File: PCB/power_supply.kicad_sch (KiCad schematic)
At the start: 25 parts, among them J1 Barrel_Jack_Switch, Q401 PMOS, U204 NCP431, U3 LDK320, U302 LMR54410DBVR, U402 TLV3542

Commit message: footprints
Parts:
- removed U402: TLV3542, w-ic:SOIC-8, symbol w-analog-ic:TLV3542
- added U403: TLV3542, w-ic:SOIC-8, symbol w-analog-ic:TLV3542
- C401: renamed from C1; footprint (none) -> Capacitor_SMD:C_0603_1608Metric
- C402: renamed from C3; footprint (none) -> Capacitor_THT:C_Radial_D6.3mm_H11.0mm_P2.50mm
- C403: renamed from C2; footprint (none) -> Capacitor_SMD:C_0603_1608Metric
- C404: renamed from C5; footprint (none) -> Capacitor_SMD:C_0603_1608Metric
- C405: renamed from C4; footprint (none) -> Capacitor_THT:C_Radial_D6.3mm_H11.0mm_P2.50mm
- C409: renamed from C6; footprint (none) -> Capacitor_SMD:C_0603_1608Metric
- C411: renamed from C7; footprint (none) -> Capacitor_SMD:C_0603_1608Metric
- C412: renamed from C8; footprint (none) -> Capacitor_SMD:C_0603_1608Metric
- D401: footprint (none) -> LED_SMD:LED_0603_1608Metric
- FB401: renamed from FB1; value FerriteBead -> 470R@100MHz; footprint (none) -> Inductor_SMD:L_0603_1608Metric; Store (none) -> https://cz.mouser.com/ProductDetail/TAIYO-YUDEN/FBMH1608HM4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
- J401: renamed from J1; footprint (none) -> w-connector:Barrel jack 6,4mm; Store (none) -> https://cz.mouser.com/ProductDetail/Adam-Tech/ADC-002-1?qs=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
- Q401: value PMOS -> DMP3125L; footprint (none) -> w-transistor:SOT23-3; Store (none) -> https://cz.mouser.com/ProductDetail/Diodes-Incorporated/DMP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
- R401, R404: footprint (none) -> Resistor_SMD:R_0603_1608Metric
- renumbered C303 to C406, C304 to C407, C308 to C408, C310 to C410, L301 to L401, U3 to U401, U302 to U402, U204 to U404
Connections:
- net +12V: now also R401.1; no longer R401.2
- net +5VA: now also U403.8 (V+)
- net GND: now also Q401.1 (G), U403.4 (V-); no longer Q401.2 (G)
- net GNDA: now also U403.1, U403.2 (-)
- net at D401.2 (A): now also R401.2; no longer R401.1
- net at R404.2, U404.1 (K), U404.2 (REF): now also U403.3 (+)
- net at J401.1: now also Q401.2 (D); no longer Q401.1 (D)
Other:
- moved on the sheet: C407, C410, Q401, R401, R402, R403

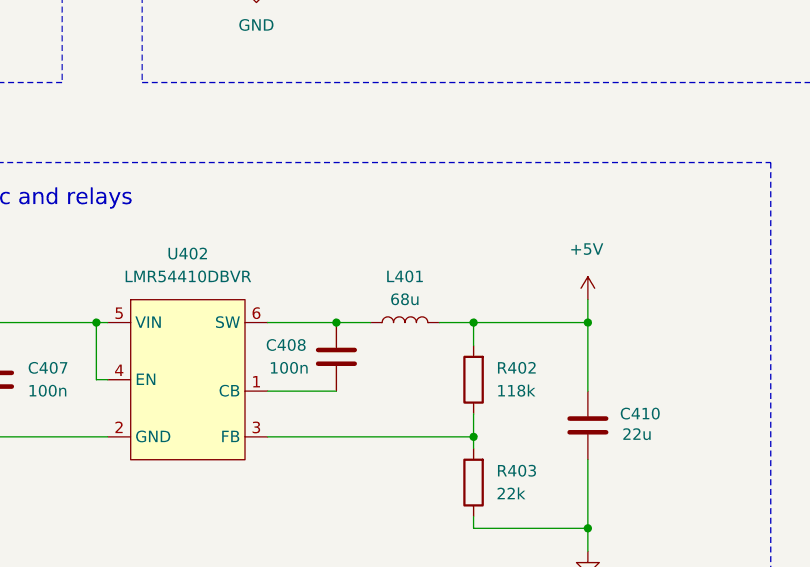
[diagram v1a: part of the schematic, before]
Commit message: footprints and overrange detector timing
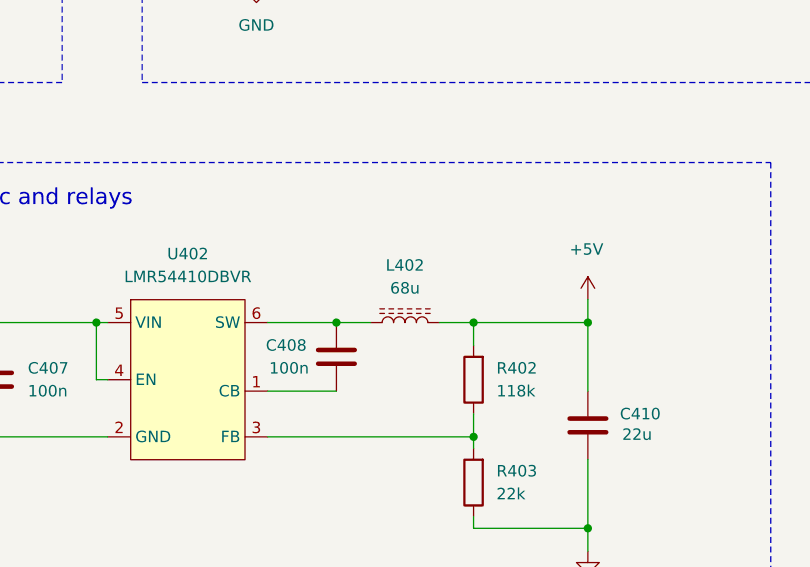
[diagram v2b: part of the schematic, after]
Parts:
- removed L401: 68u, symbol Device:L
- added L402: 68u, w-magnetics:Shielded L 6x6x4.2mm, symbol Device:L_Ferrite
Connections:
- net +5V: now also L402.2
- net at C408.2, U402.6 (SW): now also L402.1
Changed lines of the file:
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@@
-	)
-	(symbol
-		(lib_id "Device:L")
-		(at 201.93 114.3 90)
-		(unit 1)
-		(exclude_from_sim no)
-		(in_bom yes)
-		(on_board yes)
-		(dnp no)
-		(fields_autoplaced yes)
-		(property "Reference" "L401"
-			(at 201.93 109.22 90)
-			(effects
-				(font
-					(size 1.27 1.27)
-				)
-			)
-		)
-		(property "Value" "68u"
-			(at 201.93 111.76 90)
-			(effects
-				(font
-					(size 1.27 1.27)
-				)
-			)
-		)
-		(property "Footprint" ""
-			(at 201.93 114.3 0)
-			(effects
-				(font
-					(size 1.27 1.27)
-				)
-				(hide yes)
-			)
-		)
-		(property "Datasheet" "https://cz.mouser.com/datasheet/3/40/1/srn6045ta.pdf"
-			(at 201.93 114.3 0)
-			(effects
-				(font
-					(size 1.27 1.27)
-				)
-				(hide yes)
-			)
-		)
-		(property "Description" ""
-			(at 201.93 114.3 0)
-			(effects
-				(font
-					(size 1.27 1.27)
-				)
-				(hide yes)
-			)
-		)
-		(property "Store" "https://cz.mouser.com/ProductDetail/Bourns/SRN6045TA-680M?qs=Vt59ZOdFuWZwwb5da9XlfA%3D%3D"
-			(at 201.93 114.3 90)
-			(effects
-				(font
-					(size 1.27 1.27)
-				)
-				(hide yes)
-			)
-		)
-		(pin "1"
-		)
-		(pin "2"
-		)
-		(instances
-			(project "PCB"
-				(path "/8a6cedb2-c3ba-4f13-be40-fdd77ffb4e16/a8173f43-9291-44ee-92e5-00a0bb4b8099"
-					(reference "L401")
-					(unit 1)
-				)
-			)
-		)
 	)
 	(symbol
@@
 					(unit 1)
 				)
+			)
+		)
+	)
+	(symbol
+		(lib_id "Device:L_Ferrite")
+		(at 201.93 114.3 90)
+		(unit 1)
+		(exclude_from_sim no)
+		(in_bom yes)
+		(on_board yes)
+		(dnp no)
+		(fields_autoplaced yes)
+		(property "Reference" "L402"
+			(at 201.93 107.95 90)
+			(effects
+				(font
+					(size 1.27 1.27)
+				)
+			)
+		)
+		(property "Value" "68u"
+			(at 201.93 110.49 90)
+			(effects
+				(font
+					(size 1.27 1.27)
+				)
+			)
+		)
+		(property "Footprint" "w-magnetics:Shielded L 6x6x4.2mm"
+			(at 201.93 114.3 0)
+			(effects
+				(font
+					(size 1.27 1.27)
+				)
+				(hide yes)
+			)
+		)
+		(property "Datasheet" "https://cz.mouser.com/datasheet/3/40/1/srn6045ta.pdf"
+			(at 201.93 114.3 0)
+			(effects
+				(font
+					(size 1.27 1.27)
+				)
+				(hide yes)
+			)
+		)
+		(property "Description" "Inductor with ferrite core"
+			(at 201.93 114.3 0)
+			(effects
+				(font
+					(size 1.27 1.27)
+				)
+				(hide yes)
+			)
+		)
+		(property "Store" "https://cz.mouser.com/ProductDetail/Bourns/SRN6045TA-680M?qs=Vt59ZOdFuWZwwb5da9XlfA%3D%3D"
+			(at 201.93 114.3 90)
+			(effects
+				(font
+					(size 1.27 1.27)
+				)
+				(hide yes)
+			)
+		)
+		(pin "2"
+		)
+		(pin "1"
+		)
+		(instances
+			(project ""
+				(path "/8a6cedb2-c3ba-4f13-be40-fdd77ffb4e16/a8173f43-9291-44ee-92e5-00a0bb4b8099"
+					(reference "L402")
+					(unit 1)
+				)

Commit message: changes
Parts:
- removed U403: TLV3542, w-ic:SOIC-8, symbol w-analog-ic:TLV3542
- added U404: TLV9361xDBV, w-ic:SOT-23-5L, symbol Amplifier_Operational:TLV9301xDBV
- C411, C412: value 1u -> 100n
- renumbered C409 to C408, C408 to C409, L402 to L401, R404 to R402, R402 to R403, R403 to R404, U404 to U403
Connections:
- net GND2 is gone; now on net GND: C406.2, C407.2, C410.1, R404.1, U402.2 (GND)
- net +5VA: now also U404.5 (V+)
- net GND: now also C401.2, C403.2, U401.2 (GND), U404.2 (V-)
- net GNDA: now also U404.1, U404.3 (+)
- net at R402.2, U403.1 (K), U403.2 (REF): now also U404.4 (-)
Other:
- moved on the sheet: C408, C411, C412, R402, U403

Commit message: start of layout
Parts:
- removed U403: NCP431, w-ic:SOT-23, symbol Reference_Voltage:TL431DBZ
- added R405: 100k, Resistor_SMD:R_0603_1608Metric, symbol Device:R
- C410: footprint Capacitor_SMD:C_0603_1608Metric -> Capacitor_SMD:C_0805_2012Metric
- D401: footprint LED_SMD:LED_0603_1608Metric -> LED_THT:LED_D3.0mm_Clear
- R401: value 1k -> 4k7
- R402: value 4k7 -> 100k
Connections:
- net GND: now also R405.2
- net at R402.2, U404.4 (-): now also R405.1
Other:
- moved on the sheet: R402
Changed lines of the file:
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@@
 	)
 	(junction
-		(at 209.55 58.42)
+		(at 156.21 127)
 		(diameter 0)
 		(color 0 0 0 0)
 	)
 	(junction
-		(at 156.21 127)
+		(at 210.82 74.93)
 		(diameter 0)
 		(color 0 0 0 0)
@@
 	)
 	(junction
-		(at 115.57 46.99)
+		(at 210.82 58.42)
 		(diameter 0)
 		(color 0 0 0 0)
 	)
 	(junction
-		(at 86.36 46.99)
+		(at 115.57 46.99)
 		(diameter 0)
 		(color 0 0 0 0)
 	)
 	(junction
-		(at 209.55 74.93)
+		(at 86.36 46.99)
 		(diameter 0)
 		(color 0 0 0 0)
@@
 	)
 	(junction
-		(at 209.55 40.64)
-		(diameter 0)
-		(color 0 0 0 0)
-	)
-	(junction
 		(at 227.33 74.93)
 		(diameter 0)
@@
 	)
 	(junction
+		(at 210.82 40.64)
+		(diameter 0)
+		(color 0 0 0 0)
+	)
+	(junction
 		(at 209.55 114.3)
 		(diameter 0)
@@
 	(wire
 		(pts
-			(xy 209.55 40.64) (xy 227.33 40.64)
-		)
-		(stroke
-			(width 0)
-			(type default)
-		)
-	)
-	(wire
-		(pts
 			(xy 44.45 52.07) (xy 49.53 52.07)
 		)
@@
 	(wire
 		(pts
-			(xy 203.2 58.42) (xy 209.55 58.42)
-		)
-		(stroke
-			(width 0)
-			(type default)
-		)
-	)
-	(wire
-		(pts
-			(xy 203.2 64.77) (xy 203.2 58.42)
-		)
-		(stroke
-			(width 0)
-			(type default)
-		)
-	)
-	(wire
-		(pts
 			(xy 86.36 46.99) (xy 97.79 46.99)
 		)
@@
 	(wire
 		(pts
-			(xy 207.01 64.77) (xy 203.2 64.77)
-		)
-		(stroke
-			(width 0)
-			(type default)
-		)
-	)
-	(wire
-		(pts
 			(xy 237.49 55.88) (xy 246.38 55.88)
 		)
@@
 	(wire
 		(pts
-			(xy 209.55 40.64) (xy 209.55 46.99)
+			(xy 210.82 40.64) (xy 210.82 45.72)
 		)
 		(stroke
@@
 	(wire
 		(pts
-			(xy 209.55 58.42) (xy 222.25 58.42)
+			(xy 210.82 58.42) (xy 222.25 58.42)
 		)
 		(stroke
@@
 	(wire
 		(pts
+			(xy 210.82 58.42) (xy 210.82 63.5)
+		)
+		(stroke
+			(width 0)
+			(type default)
+		)
+	)
+	(wire
+		(pts
 			(xy 222.25 114.3) (xy 209.55 114.3)
 		)
@@
 	(wire
 		(pts
-			(xy 209.55 54.61) (xy 209.55 58.42)
+			(xy 210.82 53.34) (xy 210.82 58.42)
 		)
 		(stroke
@@
 	(wire
 		(pts
-			(xy 209.55 67.31) (xy 209.55 74.93)
+			(xy 210.82 71.12) (xy 210.82 74.93)
 		)
 		(stroke
@@
 		)
 	)
+	(wire
+		(pts
+			(xy 210.82 40.64) (xy 227.33 40.64)
+		)
+		(stroke
+			(width 0)
+			(type default)
+		)
+	)
 	(polyline
 		(pts
@@
 	(wire
 		(pts
-			(xy 189.23 40.64) (xy 209.55 40.64)
+			(xy 189.23 40.64) (xy 210.82 40.64)
 		)
 		(stroke
@@
 	(wire
 		(pts
-			(xy 209.55 74.93) (xy 227.33 74.93)
-		)
-		(stroke
-			(width 0)
-			(type default)
-		)
-	)
-	(wire
-		(pts
 			(xy 209.55 127) (xy 209.55 128.27)
 		)
@@
 	(wire
 		(pts
+			(xy 210.82 74.93) (xy 227.33 74.93)
+		)
+		(stroke
+			(width 0)
+			(type default)
+		)
+	)
+	(wire
+		(pts
 			(xy 222.25 53.34) (xy 218.44 53.34)
 		)
@@
 	(wire
 		(pts
-			(xy 189.23 74.93) (xy 209.55 74.93)
+			(xy 189.23 74.93) (xy 210.82 74.93)
 		)
 		(stroke
@@
 	(wire
 		(pts
-			(xy 209.55 58.42) (xy 209.55 62.23)
-		)
-		(stroke
-			(width 0)
-			(type default)
-		)
-	)
-	(wire
-		(pts
 			(xy 115.57 72.39) (xy 128.27 72.39)
 		)
@@
 			)
 		)
-		(property "Footprint" "LED_SMD:LED_0603_1608Metric"
+		(property "Footprint" "LED_THT:LED_D3.0mm_Clear"
 			(at 147.32 64.77 0)
 			(effects
@@
 	(symbol
 		(lib_id "Device:R")
-		(at 209.55 50.8 0)
+		(at 210.82 49.53 0)
 		(unit 1)
 		(exclude_from_sim no)
@@
 		(dnp no)
 		(property "Reference" "R402"
-			(at 204.47 49.53 0)
+			(at 205.74 48.26 0)
 			(effects
 				(font
@@
 			)
 		)
-		(property "Value" "4k7"
-			(at 204.47 52.07 0)
+		(property "Value" "100k"
+			(at 205.74 50.8 0)
 			(effects
 				(font
@@
 		)
 		(property "Footprint" "Resistor_SMD:R_0603_1608Metric"
-			(at 207.772 50.8 90)
+			(at 209.042 49.53 90)
 			(effects
 				(font
@@
 		)
 		(property "Datasheet" "~"
-			(at 209.55 50.8 0)
+			(at 210.82 49.53 0)
 			(effects
 				(font
@@
 		)
 		(property "Description" "Resistor"
-			(at 209.55 50.8 0)
+			(at 210.82 49.53 0)
 			(effects
 				(font
@@
 			)
 		)
-		(property "Footprint" "Capacitor_SMD:C_0603_1608Metric"
+		(property "Footprint" "Capacitor_SMD:C_0805_2012Metric"
 			(at 223.2152 121.92 0)
 			(effects
@@
 			)
 		)
-		(property "Value" "1k"
+		(property "Value" "4k7"
 			(at 152.4 55.88 0)
 			(effects
@@
 	)
 	(symbol
-		(lib_id "Reference_Voltage:TL431DBZ")
-		(at 209.55 64.77 90)
-		(unit 1)
-		(exclude_from_sim no)
-		(in_bom yes)
-		(on_board yes)
-		(dnp no)
-		(property "Reference" "U403"
-			(at 212.852 63.5 90)
-			(effects
-				(font
-					(size 1.27 1.27)
-				)
-				(justify right)
-			)
-		)
-		(property "Value" "NCP431"
-			(at 211.836 66.04 90)
-			(effects
-				(font
-					(size 1.27 1.27)
-				)
-				(justify right)
-			)
-		)
-		(property "Footprint" "w-ic:SOT-23"
-			(at 213.36 64.77 0)
-			(effects
-				(font
-					(size 1.27 1.27)
-					(italic yes)
-				)
-				(hide yes)
-			)
-		)
-		(property "Datasheet" "http://www.ti.com/lit/ds/symlink/tl431.pdf"
-			(at 209.55 64.77 0)
-			(effects
-				(font
-					(size 1.27 1.27)
-					(italic yes)
-				)
-				(hide yes)
-			)
-		)
-		(property "Description" ""
-			(at 209.55 64.77 0)
-			(effects
-				(font
-					(size 1.27 1.27)
-				)
-				(hide yes)
-			)
-		)
-		(pin "1"
-		)
-		(pin "2"
-		)
-		(pin "3"
-		)
-		(instances
-			(project "PCB"
-				(path "/8a6cedb2-c3ba-4f13-be40-fdd77ffb4e16/a8173f43-9291-44ee-92e5-00a0bb4b8099"
-					(reference "U403")
-					(unit 1)
-				)
-			)
-		)
-	)
-	(symbol
 		(lib_id "Device:C")
 		(at 257.81 66.04 0)
@@
 					(unit 1)
 				)
+			)
+		)
+	)
+	(symbol
+		(lib_id "Device:R")
+		(at 210.82 67.31 0)
+		(unit 1)
+		(exclude_from_sim no)
+		(in_bom yes)
+		(on_board yes)
+		(dnp no)
+		(property "Reference" "R405"
+			(at 205.74 66.04 0)
+			(effects
+				(font
+					(size 1.27 1.27)
+				)
+			)
+		)
+		(property "Value" "100k"
+			(at 205.74 68.58 0)
+			(effects
+				(font
+					(size 1.27 1.27)
+				)
+			)
+		)
+		(property "Footprint" "Resistor_SMD:R_0603_1608Metric"
+			(at 209.042 67.31 90)
+			(effects
+				(font
+					(size 1.27 1.27)
+				)
+				(hide yes)
+			)
+		)
+		(property "Datasheet" "~"
+			(at 210.82 67.31 0)
+			(effects
+				(font
+					(size 1.27 1.27)
+				)
+				(hide yes)
+			)
+		)
+		(property "Description" "Resistor"
+			(at 210.82 67.31 0)
+			(effects
+				(font
+					(size 1.27 1.27)
+				)
+				(hide yes)
+			)
+		)
+		(pin "2"
+		)
+		(pin "1"
+		)
+		(instances
+			(project "PCB"
+				(path "/8a6cedb2-c3ba-4f13-be40-fdd77ffb4e16/a8173f43-9291-44ee-92e5-00a0bb4b8099"
+					(reference "R405")
+					(unit 1)
+				)

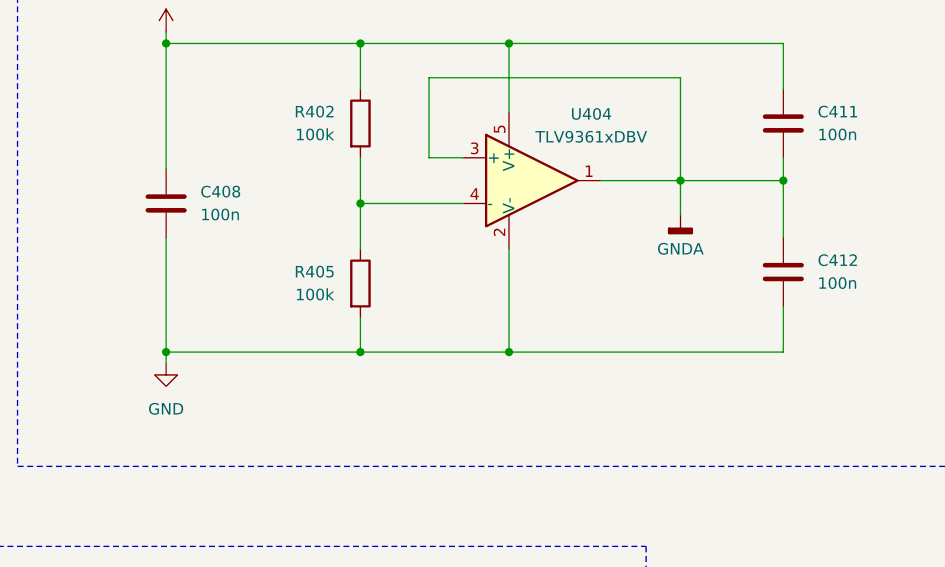
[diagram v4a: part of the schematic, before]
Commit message: changed BNC footprint
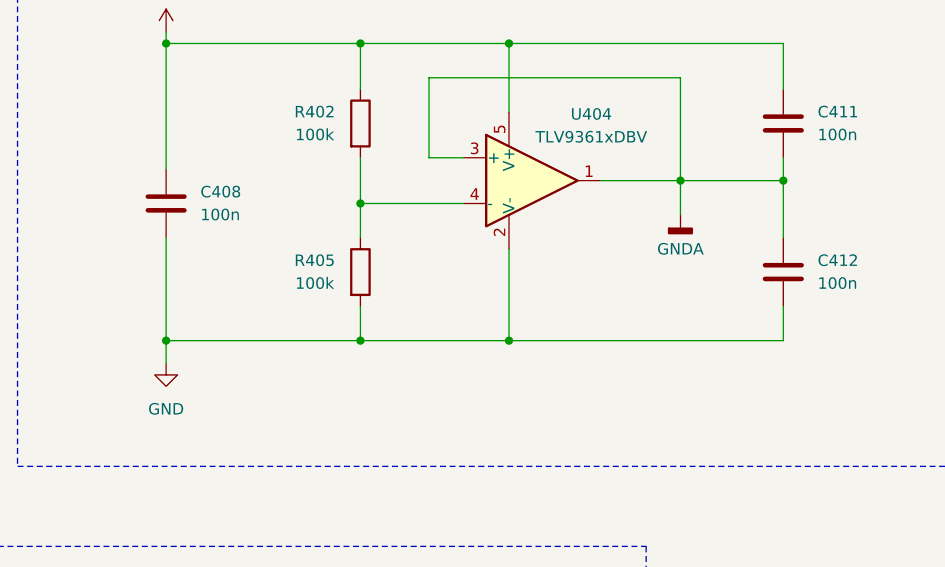
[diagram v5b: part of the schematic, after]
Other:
- moved on the sheet: R405
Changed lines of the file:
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@@
 	)
 	(junction
-		(at 210.82 74.93)
+		(at 210.82 73.66)
 		(diameter 0)
 		(color 0 0 0 0)
@@
 	)
 	(junction
-		(at 227.33 74.93)
+		(at 227.33 73.66)
 		(diameter 0)
 		(color 0 0 0 0)
@@
 	)
 	(junction
-		(at 189.23 74.93)
+		(at 189.23 73.66)
 		(diameter 0)
 		(color 0 0 0 0)
@@
 	(wire
 		(pts
-			(xy 189.23 76.2) (xy 189.23 74.93)
+			(xy 189.23 73.66) (xy 189.23 76.2)
 		)
 		(stroke
@@
 	(wire
 		(pts
-			(xy 210.82 58.42) (xy 210.82 63.5)
+			(xy 210.82 58.42) (xy 210.82 62.23)
 		)
 		(stroke
@@
 	(wire
 		(pts
-			(xy 227.33 63.5) (xy 227.33 74.93)
+			(xy 227.33 63.5) (xy 227.33 73.66)
 		)
 		(stroke
@@
 	(wire
 		(pts
-			(xy 210.82 71.12) (xy 210.82 74.93)
+			(xy 210.82 69.85) (xy 210.82 73.66)
 		)
 		(stroke
@@
 	(wire
 		(pts
-			(xy 189.23 62.23) (xy 189.23 74.93)
-		)
-		(stroke
-			(width 0)
-			(type default)
-		)
-	)
-	(wire
-		(pts
-			(xy 227.33 74.93) (xy 257.81 74.93)
+			(xy 189.23 62.23) (xy 189.23 73.66)
+		)
+		(stroke
+			(width 0)
+			(type default)
+		)
+	)
+	(wire
+		(pts
+			(xy 227.33 73.66) (xy 257.81 73.66)
 		)
 		(stroke
@@
 	(wire
 		(pts
-			(xy 210.82 74.93) (xy 227.33 74.93)
+			(xy 210.82 73.66) (xy 227.33 73.66)
 		)
 		(stroke
@@
 	(wire
 		(pts
-			(xy 189.23 74.93) (xy 210.82 74.93)
+			(xy 189.23 73.66) (xy 210.82 73.66)
 		)
 		(stroke
@@
 	(wire
 		(pts
-			(xy 257.81 69.85) (xy 257.81 74.93)
+			(xy 257.81 69.85) (xy 257.81 73.66)
 		)
 		(stroke
@@
 	(symbol
 		(lib_id "Device:R")
-		(at 210.82 67.31 0)
+		(at 210.82 66.04 0)
 		(unit 1)
 		(exclude_from_sim no)
@@
 		(dnp no)
 		(property "Reference" "R405"
-			(at 205.74 66.04 0)
+			(at 205.74 64.77 0)
 			(effects
 				(font
@@
 		)
 		(property "Value" "100k"
-			(at 205.74 68.58 0)
+			(at 205.74 67.31 0)
 			(effects
 				(font
@@
 		)
 		(property "Footprint" "Resistor_SMD:R_0603_1608Metric"
-			(at 209.042 67.31 90)
+			(at 209.042 66.04 90)
 			(effects
 				(font
@@
 		)
 		(property "Datasheet" "~"
-			(at 210.82 67.31 0)
+			(at 210.82 66.04 0)
 			(effects
 				(font
@@
 		)
 		(property "Description" "Resistor"
-			(at 210.82 67.31 0)
-			(effects
-				(font
+			(at 210.82 66.04 0)
+			(effects
+				(font
